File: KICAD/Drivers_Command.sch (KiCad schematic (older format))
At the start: 1 part

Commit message: removed legacy symbols
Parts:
- removed JP?: Jumper_NC_Dual, symbol sesame-fonctionnel-rescue:Jumper_NC_Dual-device
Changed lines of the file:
@@
 $Descr A4 11693 8268
 encoding utf-8
-Sheet 15 15
+Sheet 14 15
 Title "SESAME"
 Date ""
@@
 Text Notes 2700 2100 0    50   ~ 0
 ————————————————————————————————————————————————\nENTREE(S):\nPWM | Entree Numérique | Signal provenant du block PWM\n~PWM~ | Entree Numérique | Signal provenant du block PWM\nDir | Entrée Numérique | Sens du courant et par extension choix de la meusure Droite / Gauche | 0:Gauche -> Droite - 1:Droite -> Gaucge\nMode | Entrée Numérique  | Selecteur Boost ou buck | 0 Buck - 1 Boost\nShutdown | entree Numérique | Signal de coupure des MOS | 0: Fonctionnement Normal - 1: Disjoncté\n————————————————————————————————————————————————\nSORTIE(S):\nNmos_xx | Sortie Numérique | Signal de grille du mos xx\n\n
-$Comp
-L sesame-fonctionnel-rescue:Jumper_NC_Dual-device JP?
-U 1 1 61ED054F
-P 5750 3800
-AR Path="/61ED054F" Ref="JP?"  Part="1"
-AR Path="/60F4EAD9/61ED054F" Ref="JP?"  Part="1"
-F 0 "JP?" V 5704 3902 50  0000 L CNN
-F 1 "Jumper_NC_Dual" V 5795 3902 50  0000 L CNN
-F 2 "" H 5750 3800 50  0001 C CNN
-F 3 "~" H 5750 3800 50  0001 C CNN
-	1    5750 3800
-	0    -1   -1   0
-$EndComp
 $EndSCHEMATC

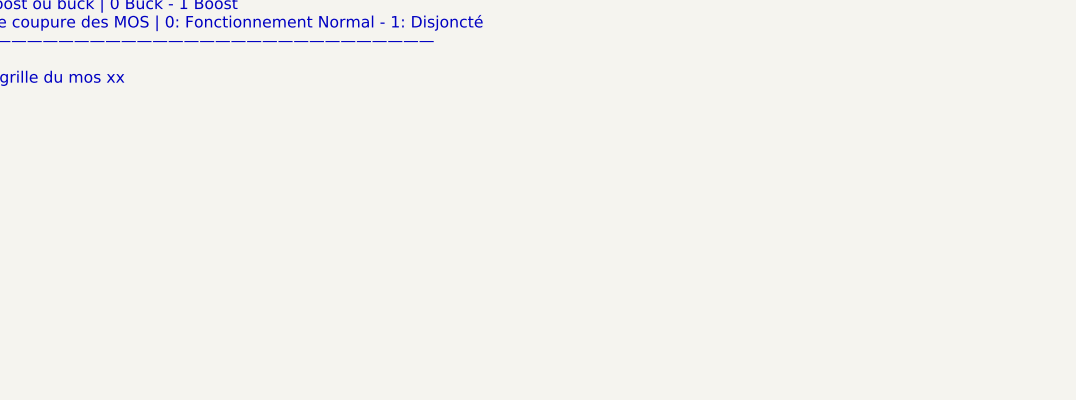
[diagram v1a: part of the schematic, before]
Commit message: labels dans les blocks
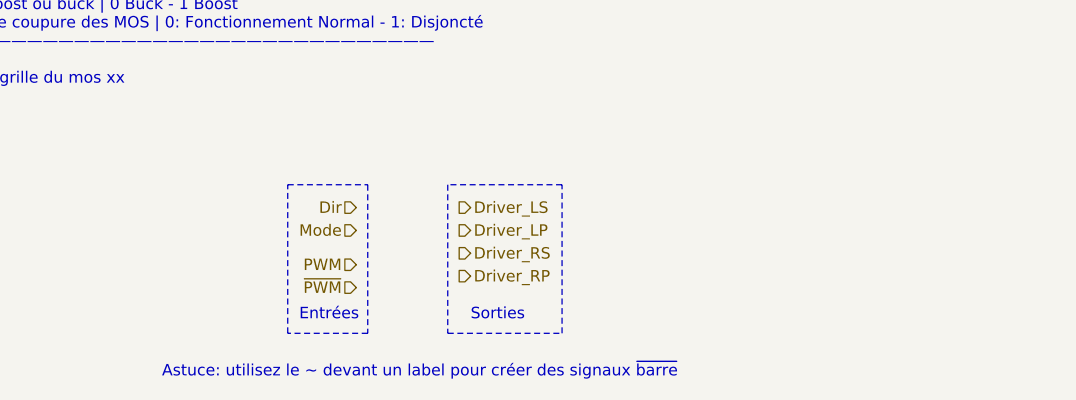
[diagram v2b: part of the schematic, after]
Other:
- note added: "Astuce: utilisez le ~~ devant un label pour créer des signaux ~barre"
- note added: "Entrées"
- note added: "Sorties"
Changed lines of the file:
@@
 $Descr A4 11693 8268
 encoding utf-8
-Sheet 14 15
+Sheet 13 15
 Title "SESAME"
 Date ""
@@
 Text Notes 2700 2100 0    50   ~ 0
 ————————————————————————————————————————————————\nENTREE(S):\nPWM | Entree Numérique | Signal provenant du block PWM\n~PWM~ | Entree Numérique | Signal provenant du block PWM\nDir | Entrée Numérique | Sens du courant et par extension choix de la meusure Droite / Gauche | 0:Gauche -> Droite - 1:Droite -> Gaucge\nMode | Entrée Numérique  | Selecteur Boost ou buck | 0 Buck - 1 Boost\nShutdown | entree Numérique | Signal de coupure des MOS | 0: Fonctionnement Normal - 1: Disjoncté\n————————————————————————————————————————————————\nSORTIE(S):\nNmos_xx | Sortie Numérique | Signal de grille du mos xx\n\n
+Text HLabel 6100 2550 2    50   Output ~ 0
+Driver_LS
+Text HLabel 6100 2650 2    50   Output ~ 0
+Driver_LP
+Text HLabel 6100 2750 2    50   Output ~ 0
+Driver_RS
+Text HLabel 6100 2850 2    50   Output ~ 0
+Driver_RP
+Text HLabel 5650 2550 0    50   Input ~ 0
+Dir
+Text HLabel 5650 2650 0    50   Input ~ 0
+Mode
+Text HLabel 5650 2800 0    50   Input ~ 0
+PWM
+Text HLabel 5650 2900 0    50   Input ~ 0
+~PWM
+Text Notes 5400 3050 0    50   ~ 0
+Entrées
+Text Notes 6150 3050 0    50   ~ 0
+Sorties
+Wire Notes Line
+	6050 3100 6550 3100
+Wire Notes Line
+	6550 3100 6550 2450
+Wire Notes Line
+	6550 2450 6050 2450
+Wire Notes Line
+	6050 2450 6050 3100
+Wire Notes Line
+	5700 2450 5700 3100
+Wire Notes Line
+	5700 3100 5350 3100
+Wire Notes Line
+	5350 3100 5350 2450
+Wire Notes Line
+	5350 2450 5700 2450
+Text Notes 4800 3300 0    50   ~ 0
+Astuce: utilisez le ~~ devant un label pour créer des signaux ~barre
 $EndSCHEMATC

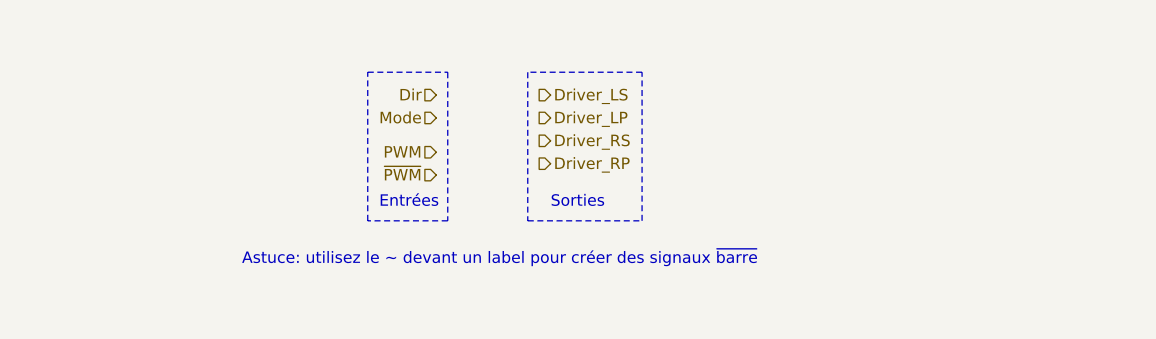
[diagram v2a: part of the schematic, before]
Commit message: finished measure selector
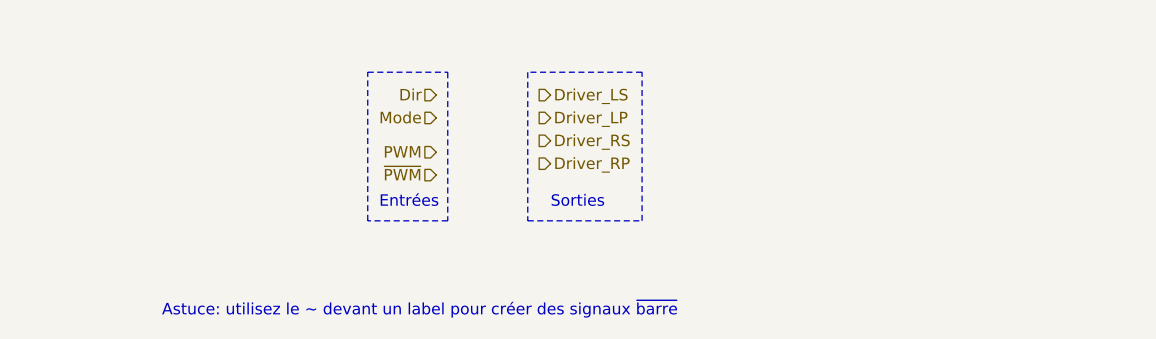
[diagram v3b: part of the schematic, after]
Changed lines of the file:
@@
 Wire Notes Line
 	5350 2450 5700 2450
-Text Notes 4800 3300 0    50   ~ 0
+Text Notes 4450 3525 0    50   ~ 0
 Astuce: utilisez le ~~ devant un label pour créer des signaux ~barre
 $EndSCHEMATC

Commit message: Nearly finished Driver cmd
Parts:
- added R? (x4): R, symbol Device:R
- added U?: 4011, symbol sesame-fonctionnel-rescue:CD4053B-Analog_Switch
- added U? (x5): 4011, symbol 4xxx:4011
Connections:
- net Dir: now also U?.1, U?.5
- net Driver_LP: now also R?.1, U?.2 (B0)
- net Driver_LS: now also R?.2, U?.12 (A0)
- net Driver_RP: now also R?.1, U?.1 (B1)
- net Driver_RS: now also R?.2, U?.13 (A1)
- net Mode: now also U?.2, U?.9
- net PWM: now also U?.14 (A)
- net ~PWM: now also U?.15 (B)
- new net: U?.10 (S2), U?.11, U?.11 (S1)
- new net: U?.3, U?.6, U?.8
- new net: U?.10, U?.13
- new net: U?.12, U?.4
- new net GND: R?.2, R?.2, U?.3 (C1), U?.4 (C), U?.5 (C0), U?.6 (INH), U?.7 (VEE), U?.7 (VSS), U?.8 (VSS), U?.9 (S3)
- new net VCC: R?.1, R?.1, U?.14 (VDD), U?.16 (VDD)
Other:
- note removed: "Entrées"
- note removed: "Sorties"

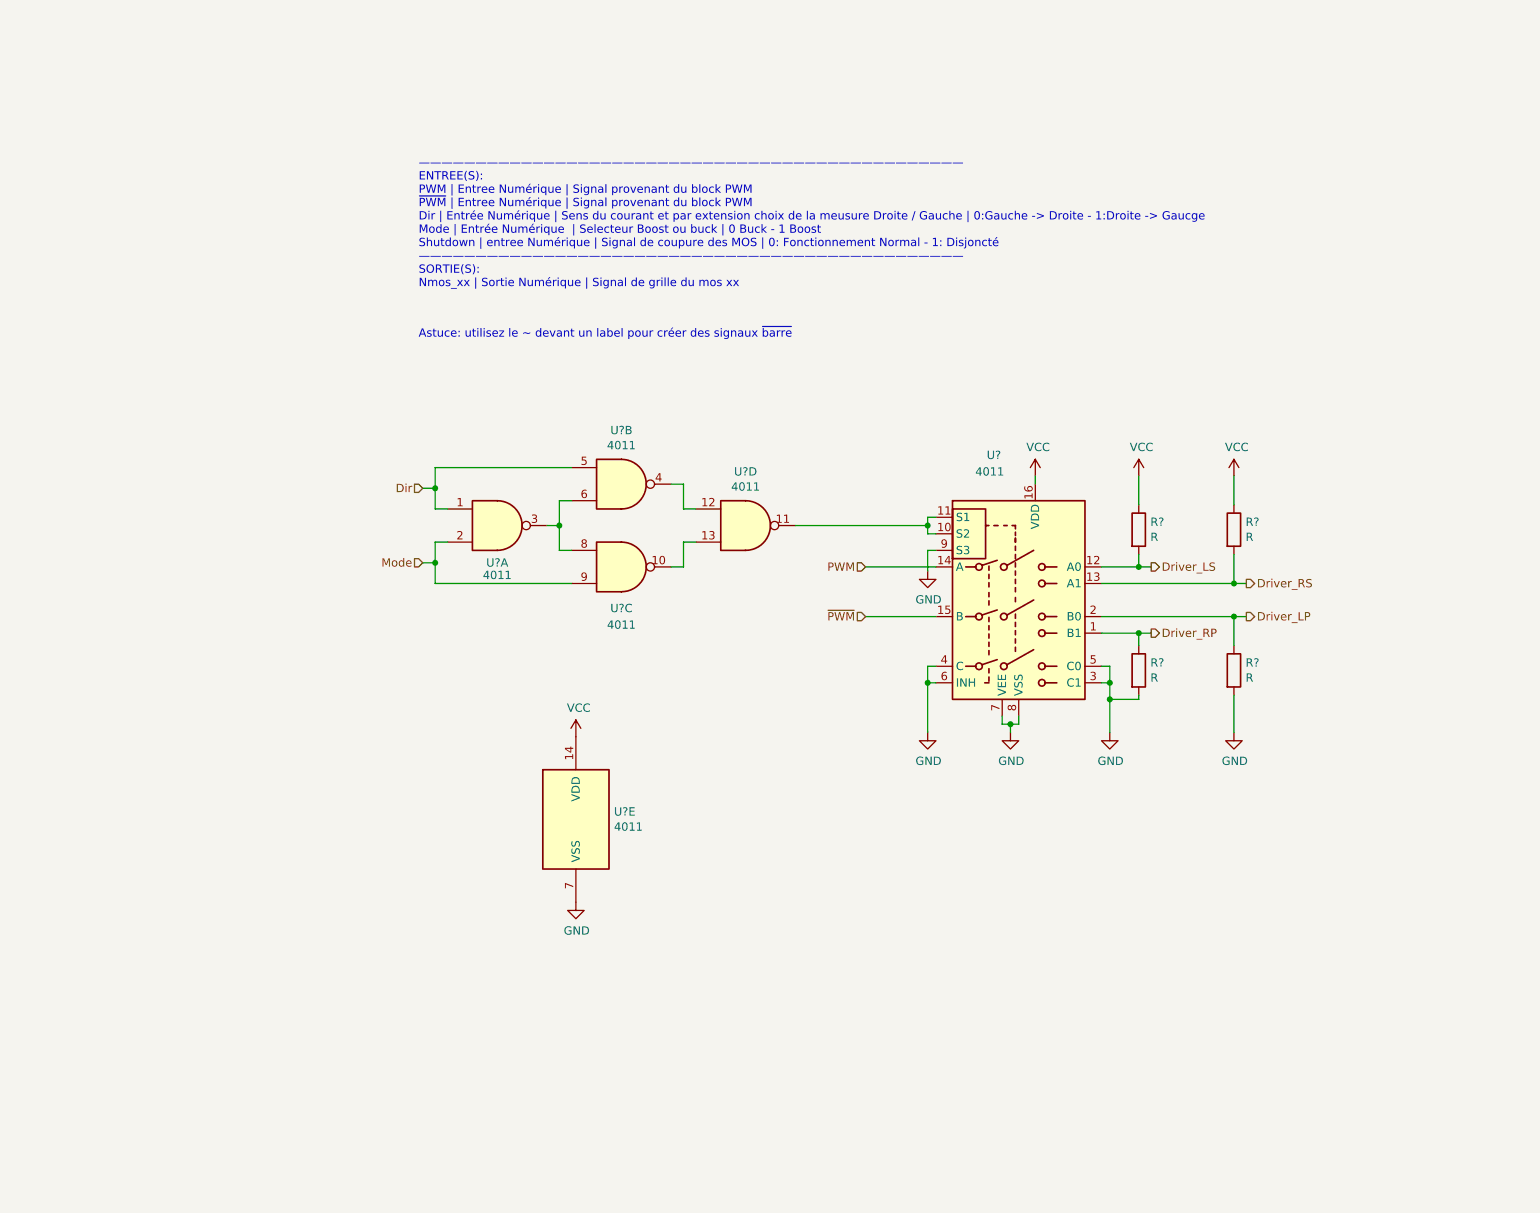
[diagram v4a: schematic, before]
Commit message: update header + redraw Driver CMD
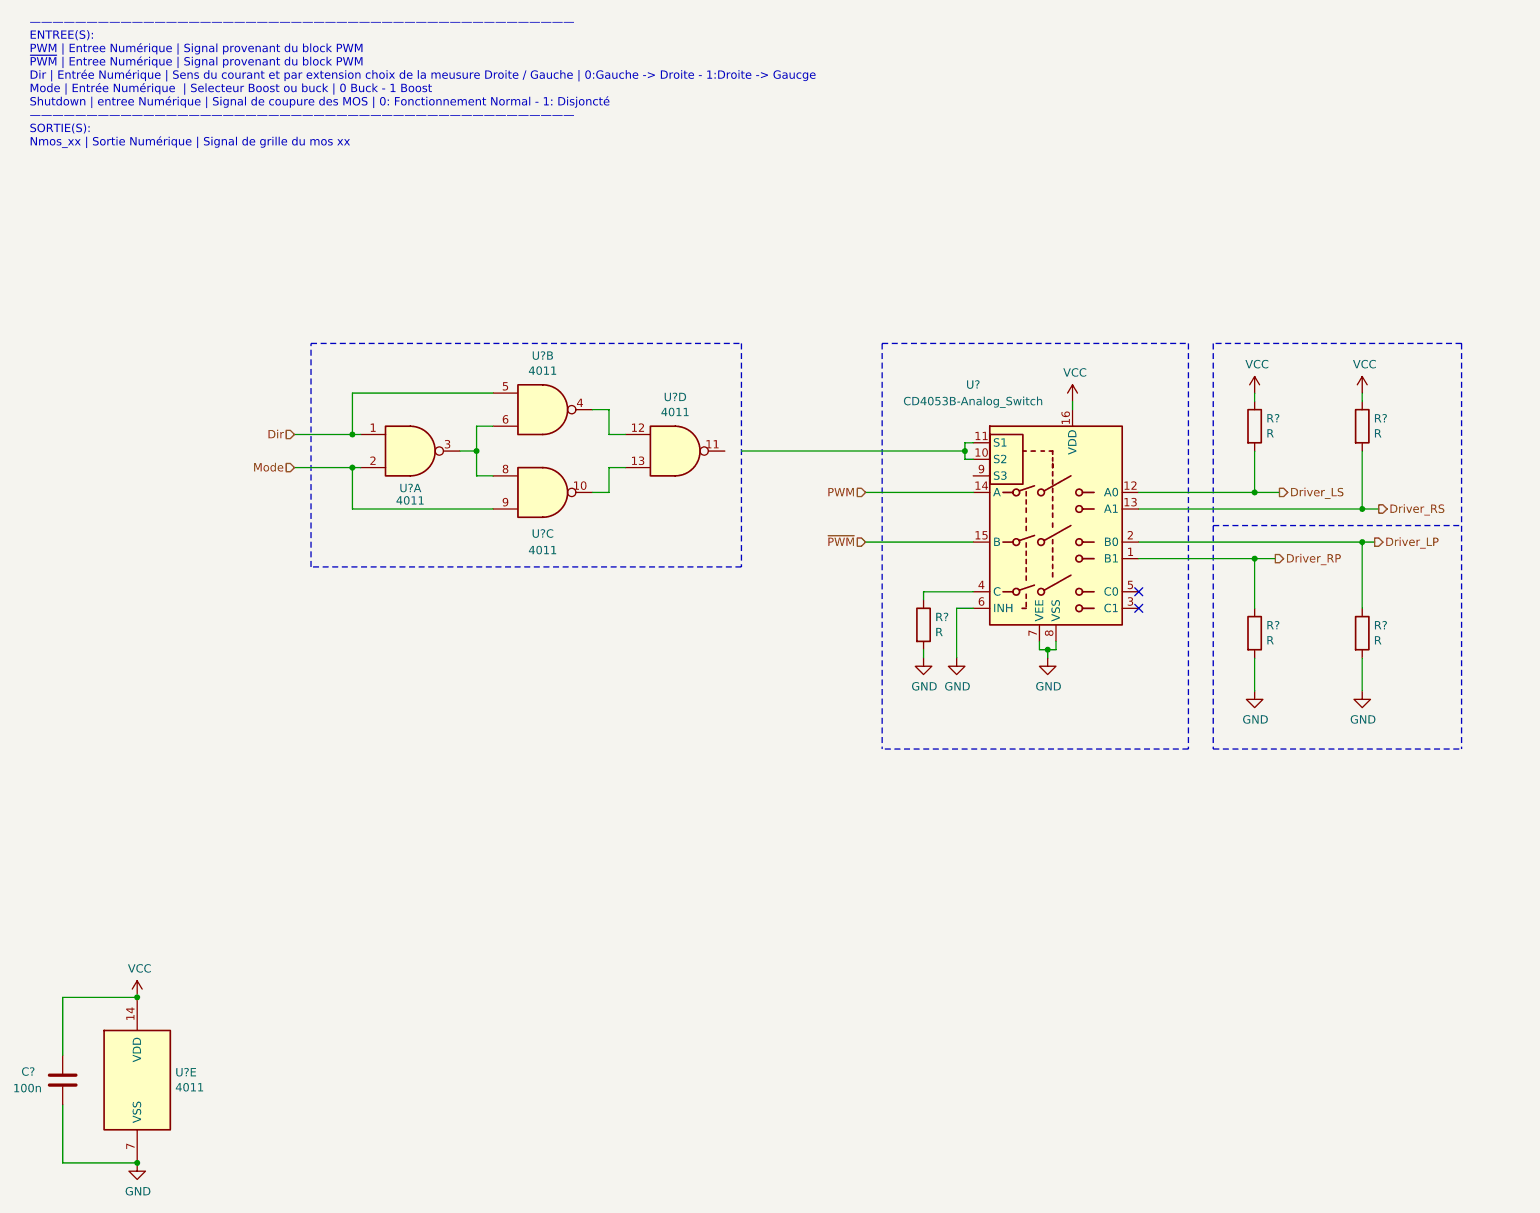
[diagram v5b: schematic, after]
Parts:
- removed R? (x2): R, symbol Device:R
- removed U?: 4011, symbol sesame-fonctionnel-rescue:CD4053B-Analog_Switch
- removed U?: 4011, symbol 4xxx:4011
- added C?: 100n, symbol Device:C
- added R? (x3): R, symbol Device:R
- added U?: 4011, symbol 4xxx:4011
- added U?: CD4053B-Analog_Switch, symbol sesame-fonctionnel-rescue:CD4053B-Analog_Switch
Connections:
- net Driver_LP: now also U?.2 (B0)
- net Driver_LS: now also R?.2, U?.12 (A0)
- net Driver_RP: now also U?.1 (B1)
- net Driver_RS: now also R?.2, U?.13 (A1)
- net GND: now also C?.2, R?.2, U?.6 (INH), U?.7 (VEE), U?.7 (VSS), U?.8 (VSS)
- net PWM: now also U?.14 (A)
- net VCC: now also C?.1, R?.1, R?.1, U?.14 (VDD), U?.16 (VDD)
- net ~PWM: now also U?.15 (B)
- new net: R?.1, U?.4 (C)
- new net: U?.10 (S2), U?.11 (S1)
- no-connect marks 0 -> 2
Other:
- note removed: "Astuce: utilisez le ~~ devant un label pour créer des signaux ~barre"
- moved on the sheet: R?, U?A, U?B, U?C, U?D
